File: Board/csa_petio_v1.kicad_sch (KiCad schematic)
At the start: 14 parts, among them IC12 7417N, IC3 7400N, P1 C64KEYB, P3 PETUSERPORT, P5 CBMTAPE, P6 CBMTAPE, P7 PETKEYBD, P8 PETKEYBDSUBD

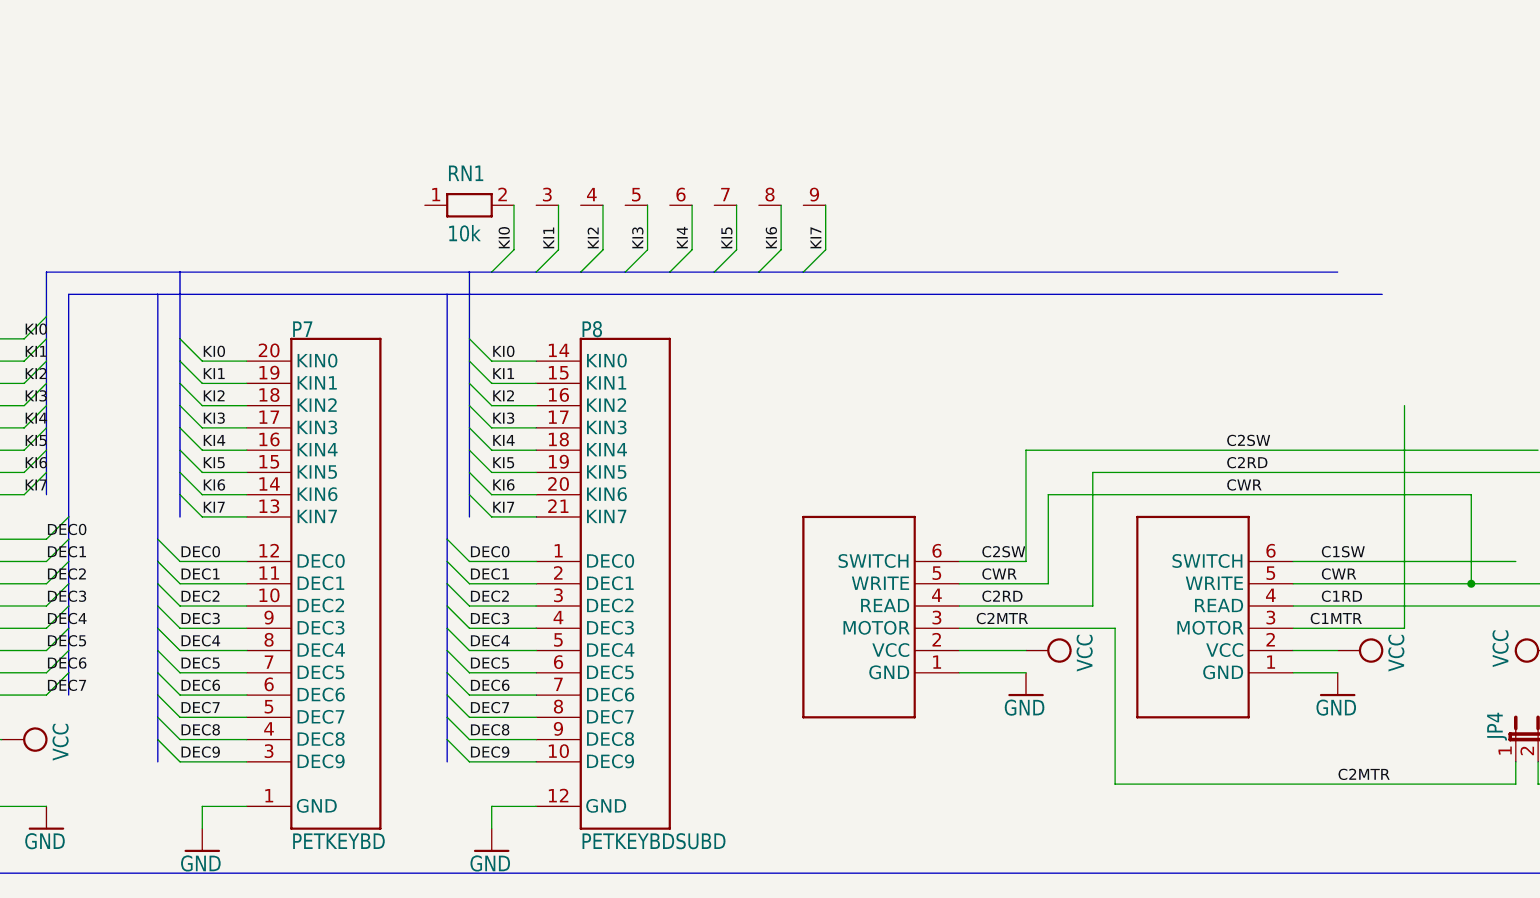
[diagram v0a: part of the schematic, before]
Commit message: adding keyboard, serial IEC
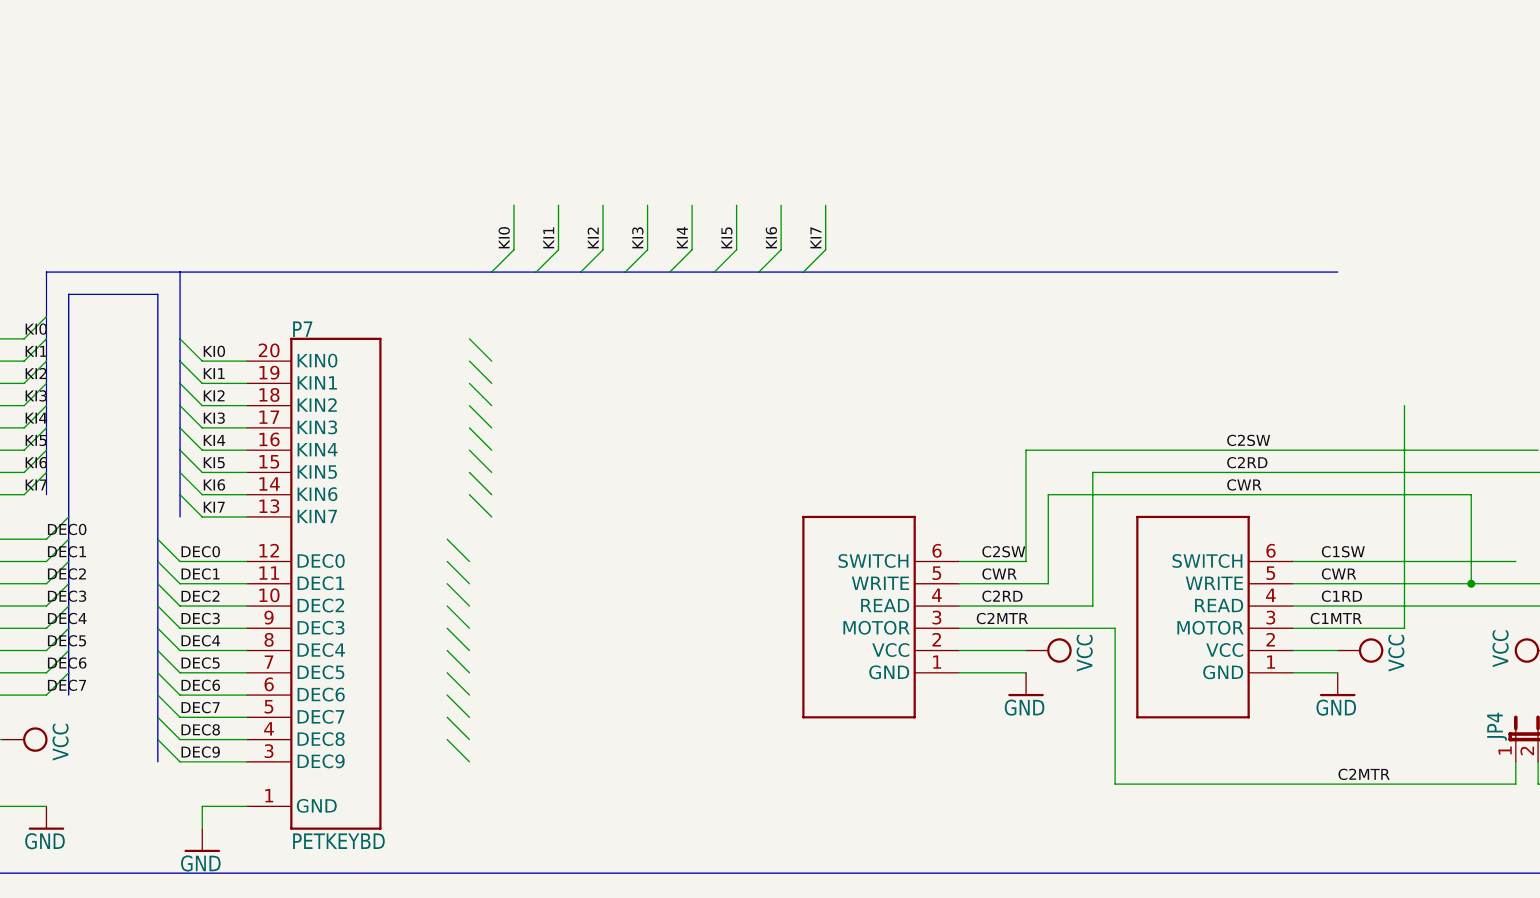
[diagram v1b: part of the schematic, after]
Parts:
- removed P8: PETKEYBDSUBD, csa_petio_v1:SUBD25F, symbol csa_petio_v1-eagle-import:PETKEYBDSUBD
- removed RN1: 10k, csa_petio_v1:RN-9, symbol csa_petio_v1-eagle-import:RN08

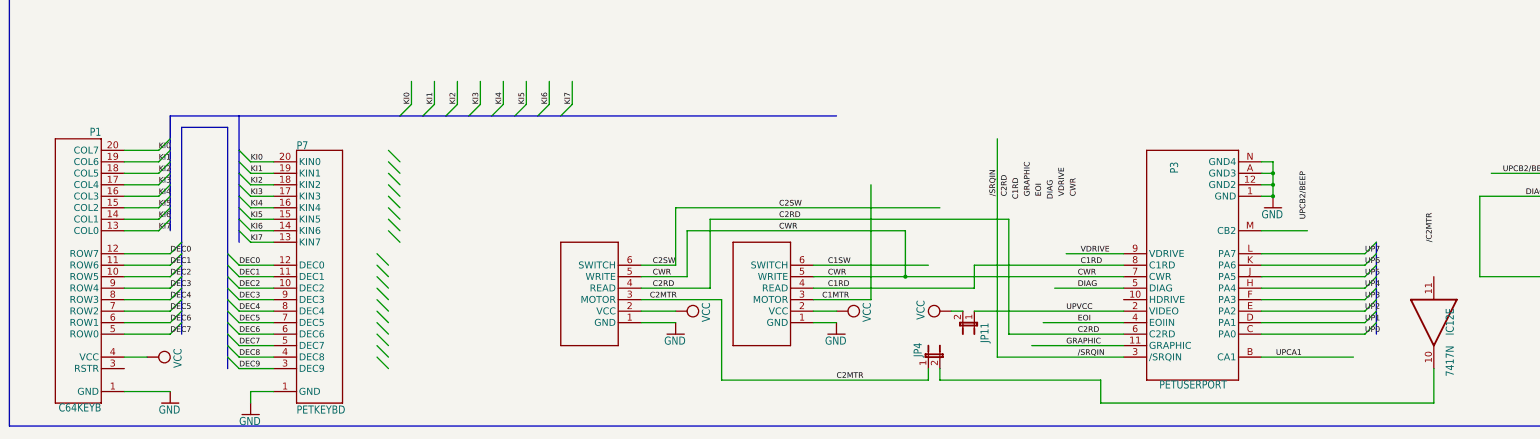
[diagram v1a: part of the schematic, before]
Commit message: add serial, SPI-10-5V
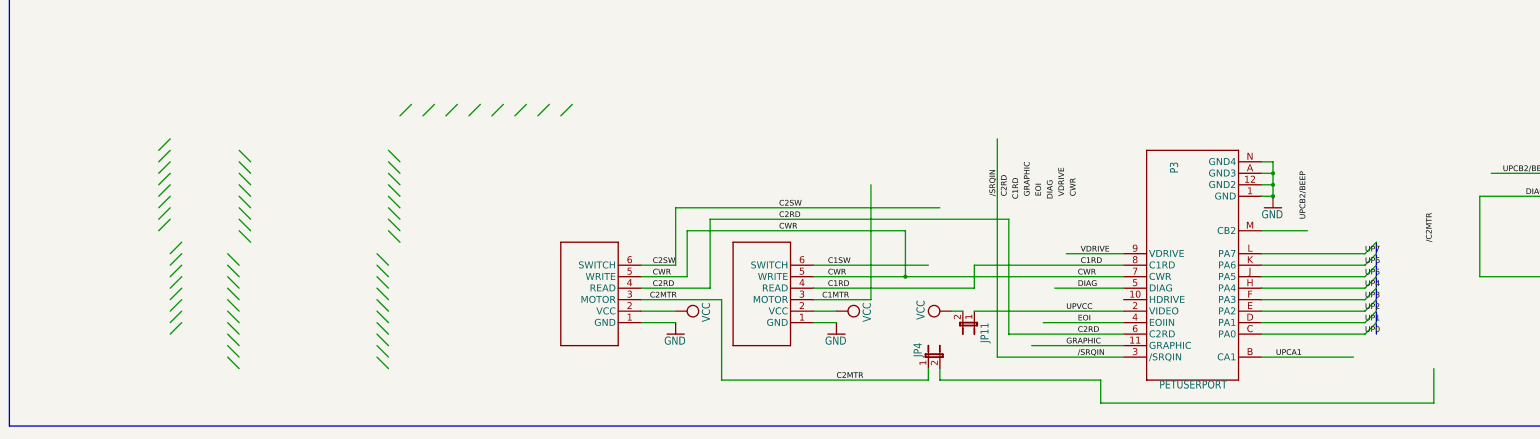
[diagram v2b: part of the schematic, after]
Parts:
- removed IC12: 7417N, csa_petio_v1:DIL14, symbol csa_petio_v1-eagle-import:7417N
- removed P1: C64KEYB, csa_petio_v1:C64KEYB, symbol csa_petio_v1-eagle-import:C64KEYB
- removed P7: PETKEYBD, csa_petio_v1:C64KEYB, symbol csa_petio_v1-eagle-import:PETKEYBD

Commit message: schematics 1st full rev
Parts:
- removed BEEP1: PIEZOBEEPERPIEZO, csa_petio_v1:PIEZOBEEPER, symbol csa_petio_v1-eagle-import:PIEZOBEEPERPIEZO
- removed IC3: 7400N, csa_petio_v1:DIL14, symbol csa_petio_v1-eagle-import:7400N
- removed JP11, JP4: JP1E, csa_petio_v1:JP1, symbol csa_petio_v1-eagle-import:JP1E
- removed P3: PETUSERPORT, csa_petio_v1:FLAT24, symbol csa_petio_v1-eagle-import:PETUSERPORT
- removed P5, P6: CBMTAPE, csa_petio_v1:JP6, symbol csa_petio_v1-eagle-import:CBMTAPE
- removed R6: 10, csa_petio_v1:0207_10, symbol csa_petio_v1-eagle-import:R-EU_0207/10
- removed U$2: TASTER, csa_petio_v1:TASTER, symbol csa_petio_v1-eagle-import:TASTER
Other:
- added sheet Userport (userport.kicad_sch)
- note removed: "(C) A. Fachat"
- note removed: "CSA-PETIO-V1.3B"
- note removed: "CSA-PETIO-V1.3B-20240214"
